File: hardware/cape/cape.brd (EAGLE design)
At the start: 86.4 x 54.6 mm, 159 parts, among them IC1 AD8422BRMZ, IC10 DAC8562_DGS_10, IC11 CAT24C256WI-GT3, IC12 LM27762DSSR, IC13 BQ25505, IC14 SN74LV4T125PWR, IC15 LMP7701MF, IC16 TXB0304RUTR, IC2 OPA2388DGK8_L, IC3 AD8422BRMZ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

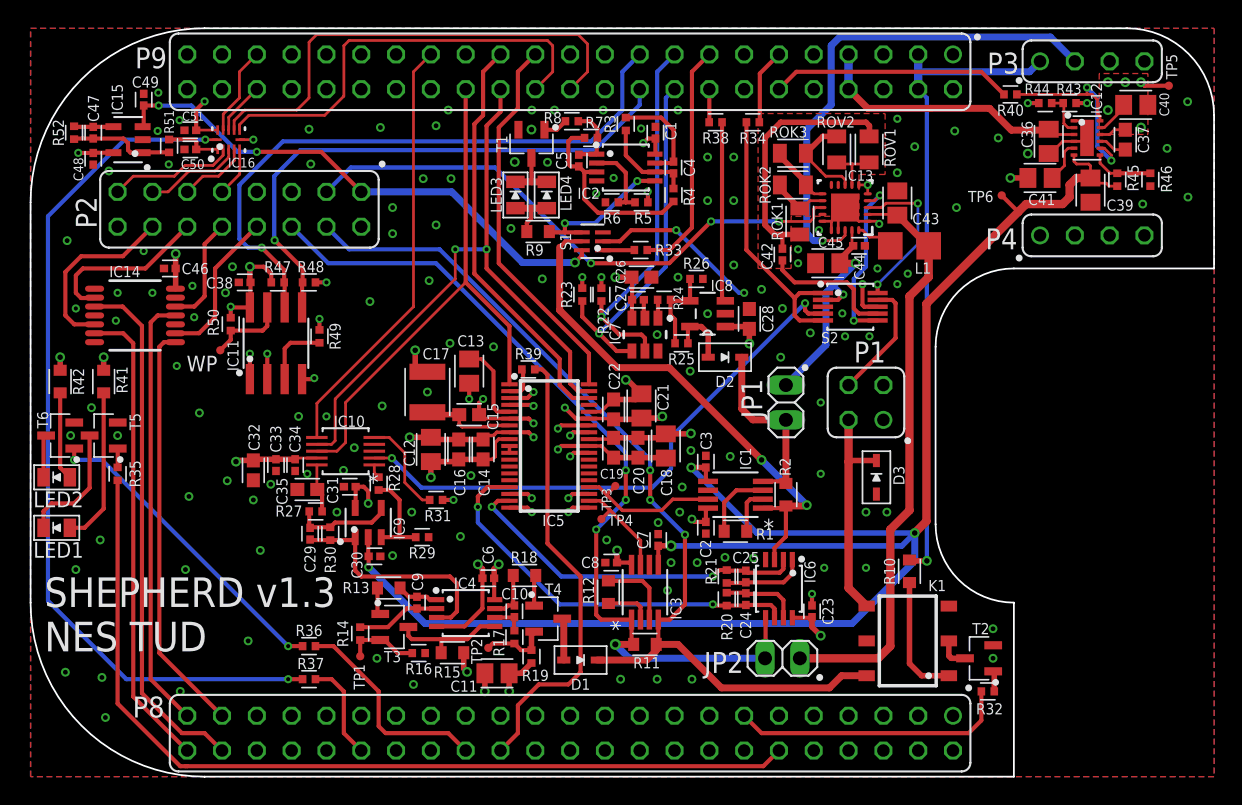
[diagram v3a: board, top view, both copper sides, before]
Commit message: hardware: cape: reverted to BQ25504, fixed booting bug and added logo
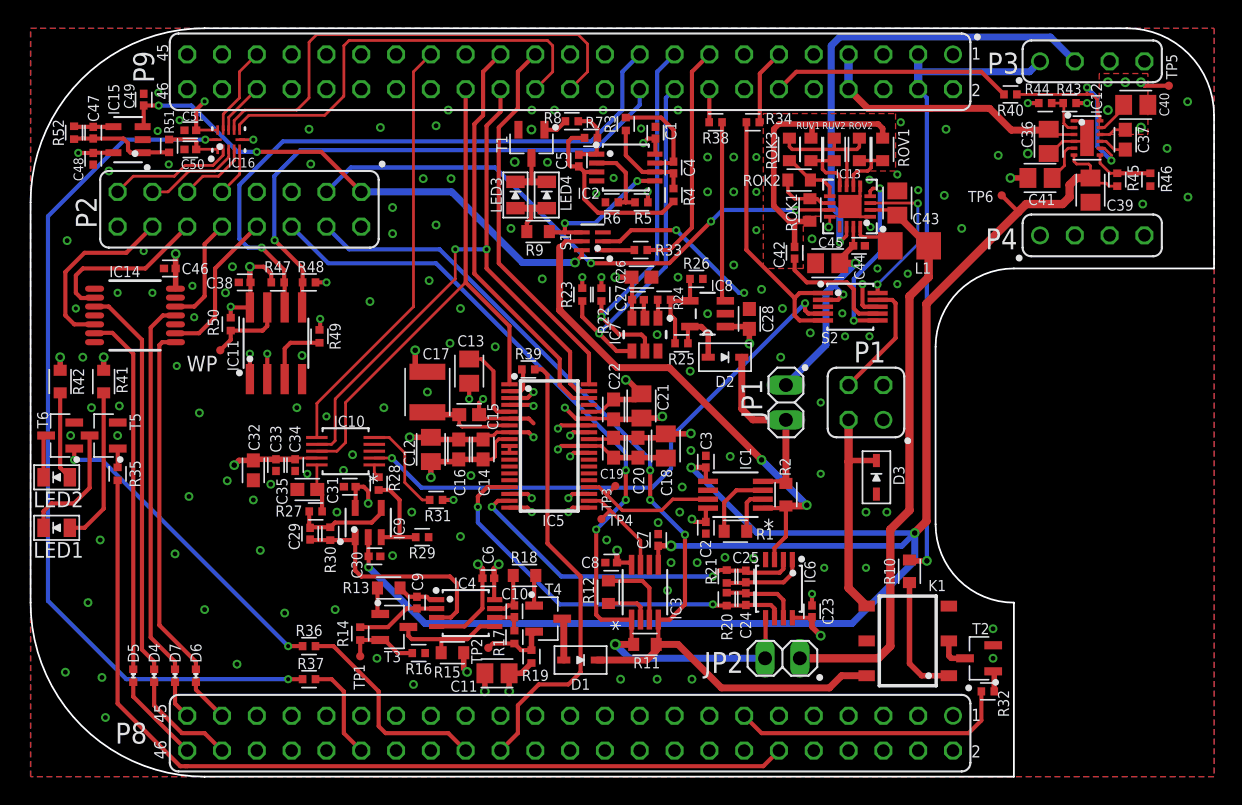
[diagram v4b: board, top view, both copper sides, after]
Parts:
- added D4, D5, D6, D7: ACDBQC0130L-HF0402, shepherd:DIOC1005X55N
- added RUV1: 5.62M, mylib:RESC1608X55
- added RUV2: 3.6M, mylib:RESC1608X55
- IC13: value BQ25505 -> BQ25504_RGT_16; device mylib:RGR0020A -> shepherd:RGT16_1P7X1P7
- ROK1, ROK2, ROK3, ROV1, ROV2: device mylib:RESC2012X65 -> mylib:RESC1608X55
- moved U$2 10.0 mm to (4.01, 8.23)
- moved ROV2 1.65 mm to (60.5, 45.8)
- moved ROK1 1.12 mm to (56.9, 41.4)
- moved ROV1 0.99 mm to (62.2, 45.8)
- moved C42 0.90 mm to (55.8, 38.2)
- moved ROK2 0.58 mm to (56.1, 43.5)
- moved U$3 0.57 mm to (68.8, 45.6)
- moved ROK3 0.38 mm to (55.4, 45.8), turned to 90 degrees
- moved IC13 0.36 mm to (59.8, 41.6)
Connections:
- removed net VBAT_PRI: IC13.14
- removed net VB_SEC_ON_N: IC13.9
- new net N$43: D4.1, IC14.3
- new net N$47: D5.1, IC14.6
- new net N$50: D6.1, IC14.8
- new net N$51: D7.1, IC14.11
- new net V_VBAT_UV: IC13.8, RUV1.2, RUV2.1
- net GND: now also IC13.12, IC13.13, RUV1.1; no longer IC13.15, IC13.16, IC13.21, IC13.6
- net GPIO0_BB: now also D7.2; no longer IC14.11
- net GPIO1_BB: now also D5.2; no longer IC14.6
- net GPIO2_BB: now also D6.2; no longer IC14.8
- net GPIO3_BB: now also D4.2; no longer IC14.3
- net N$19: now also IC13.16; no longer IC13.20
- net V_BAT: now also IC13.14; no longer IC13.18
- net V_BATOK: now also IC13.11; no longer IC13.13
- net V_OK_HYST: now also IC13.9; no longer IC13.11
- net V_OK_PROG: now also IC13.10; no longer IC13.12
- net V_STR: now also IC13.15; no longer IC13.19
- net V_VBAT_OV: now also IC13.6; no longer IC13.7
- net V_VRDIV: now also IC13.7, RUV2.2; no longer IC13.8
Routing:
- net GPIO3_BB: track 38.4 -> 8.01 mm
- net GPIO0_BB: track 31.8 -> 2.82 mm
- net N$43: track 0.00 -> 28.9 mm
- net GPIO1_BB: track 34.5 -> 6.62 mm
- net N$51: track 0.00 -> 27.8 mm
- net GPIO2_BB: track 30.1 -> 3.24 mm
- net N$47: track 0.00 -> 26.5 mm
- net N$50: track 0.00 -> 26.0 mm
- net V_VBAT_UV: track 0.00 -> 4.55 mm
- net V_VRDIV: track 6.93 -> 10.1 mm
- net V_BAT: track 36.8 -> 34.7 mm
- net GND: track 101.1 -> 99.4 mm, vias 155 -> 161
- net V_CREF: track 9.79 -> 9.03 mm
- net VREF_SAMP: track 12.7 -> 13.3 mm
- net VDD: track 134.2 -> 134.8 mm
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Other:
- board text added: "1"
- board text added: "2"
- board text added: "45"
- board text added: "46"
- board text added: "SHEPHERD v1.4 NES TUD"
- board text removed: "SHEPHERD v1.3 NES TUD"

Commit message: hardware: replaced LDO diode with switch connected to PRU+ARM. Added connector for illuminated button.
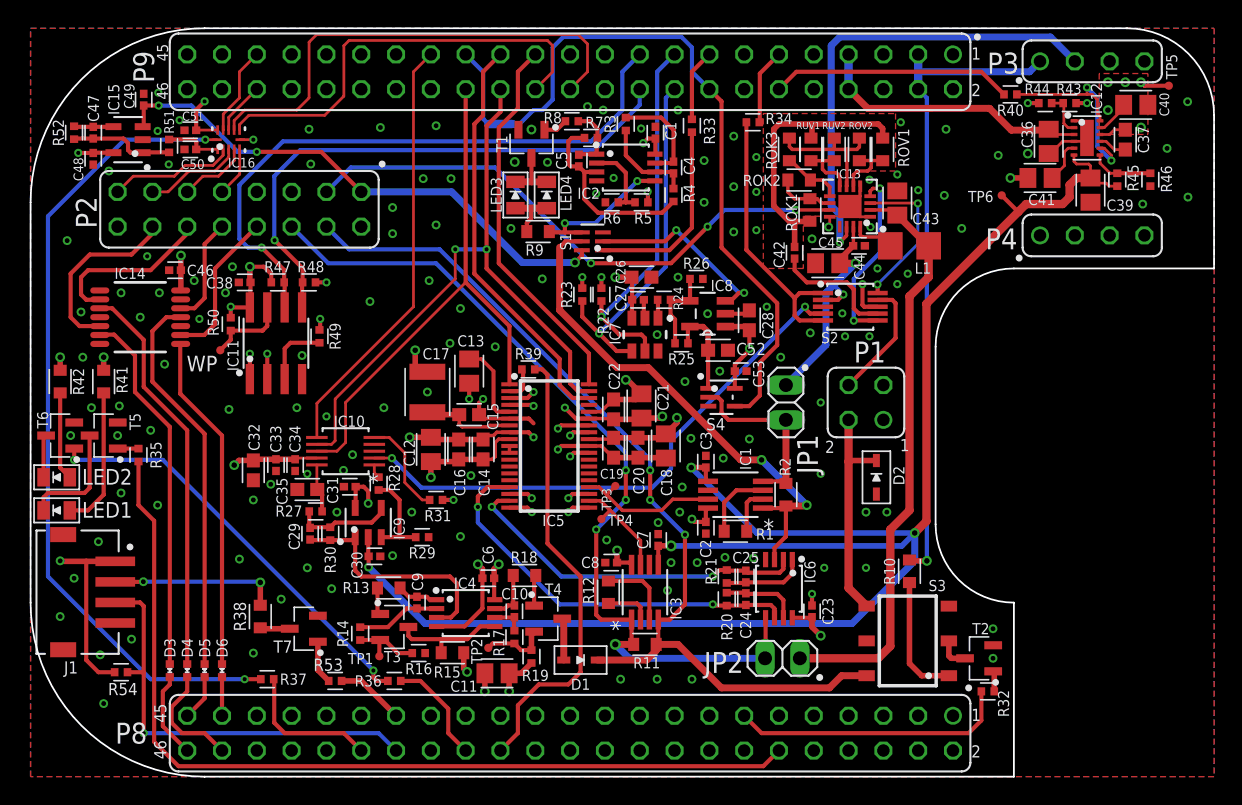
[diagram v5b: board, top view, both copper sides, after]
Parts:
- removed D7: ACDBQC0130L-HF0402, shepherd:DIOC1005X55N
- added C52: 1u, shepherd:CAPC1608X95
- added C53: 0.1u, mylib:CAPC1005X55
- added J1: JST_S4B-ZR-SM4A-TFJST_S4B-ZR-SM4A-TF_0_0, shepherd:JST_S4B-ZR-SM4A-TF_0
- added R53: 510, mylib:RESC1005X40
- added R54: 10k, mylib:RESC1005X40
- added S4: TMUX1101DCK, shepherd:DCK5
- added T7: SI2374DSSOT23-VSHAY, mylib:SOT95P237X112-3
- D2: value BAT43WS-HE3SOD-323 -> BZX384B5V1
- D3: value BZX384B5V1 -> ACDBQC0130L-HF0402; device mylib:SOD2513X110 -> shepherd:DIOC1005X55N
- R38: value 510 -> 220; device mylib:RESC1005X40 -> mylib:RESC1608X55
- moved D3 53.5 mm to (10.2, 7.75)
- moved R38 49.0 mm to (16.8, 11.7), turned to 90 degrees
- moved D2 14.1 mm to (61.7, 21.8), turned to 270 degrees
- moved R33 9.81 mm to (48.3, 47.5), turned to 270 degrees
- moved R36 6.72 mm to (26.5, 6.99)
- moved D5 5.22 mm to (12.7, 7.75)
- moved R37 3.05 mm to (17.3, 7.11)
- moved D4 2.44 mm to (11.4, 7.75)
- moved R35 2.05 mm to (7.87, 23.5)
- moved U$2 2.05 mm to (4.26, 6.20)
- moved D6 1.94 mm to (14.0, 7.75)
- moved TP1 1.40 mm to (25.5, 8.79)
- moved LED1 1.27 mm to (1.91, 19.4)
- moved C46 0.40 mm to (10.5, 37.0)
- moved IC14 0.40 mm to (8.00, 33.5)
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- renumbered K1 to S3
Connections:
- new net BUTTON_LED_OD: J1.2, R38.2
- new net LED_BUTTON: R53.1, T7.1
- new net N$53: R38.1, T7.3
- new net SENSE_BUTTON: J1.3, P8.34, R54.2
- net +3V3: now also J1.1, R54.1
- net EN_V_FIX: now also P9.16, P9.29, S4.4; no longer IC8.3, R38.2
- net GND: now also C52.2, C53.2, D2.2, J1.4, J1.5, J1.6, S4.3, T7.2; no longer D3.2
- net GPIO0_BB: now also D5.2; no longer D7.2
- net GPIO1_BB: now also D3.2; no longer D5.2
- net N$14: now also R33.1; no longer R33.2
- net N$28: now also P8.33, R53.2; no longer P9.16, R38.1
- net N$47: now also D3.1; no longer D5.1
- net N$51: now also D5.1; no longer D7.1
- net N$7: now also C52.1, S4.1; no longer D2.2
- net SLCT_LOAD: now also R33.2; no longer R33.1
- net VDD: now also C53.1, IC8.3, S4.5
- net V_H: now also D2.1; no longer D3.1
- net V_LD_SHT+: now also S4.2; no longer D2.1
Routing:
- net EN_V_FIX: track 13.1 -> 56.5 mm
- net SENSE_BUTTON: track 0.00 -> 31.6 mm, vias 0 -> 1
- net +3V3: track 80.1 -> 103.0 mm, vias 15 -> 16
- net BUTTON_LED_OD: track 0.00 -> 12.3 mm, vias 0 -> 2
- net SLCT_LOAD: track 2.30 -> 14.1 mm
- net N$14: track 17.1 -> 5.26 mm
- net N$38: track 15.6 -> 7.88 mm
- net LED_USR2: track 23.1 -> 30.7 mm
- net VDD: track 134.8 -> 139.7 mm
- net EN_LVLCNV: track 63.7 -> 59.6 mm
- net LED_BUTTON: track 0.00 -> 3.19 mm
- net N$30: track 7.28 -> 10.4 mm
- net N$28: track 2.42 -> 5.03 mm
- net N$7: track 4.56 -> 6.91 mm
- net N$53: track 0.00 -> 2.18 mm
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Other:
- board text added: "SHEPHERD v1.5 NES TUD"
- board text removed: "SHEPHERD v1.4 NES TUD"

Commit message: hardware: minor revisions on cape silkscreen
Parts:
- moved U$2 0.28 mm to (4.39, 6.45)
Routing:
- net EN_V_FIX: track 56.5 -> 57.1 mm, vias 0 -> 1
